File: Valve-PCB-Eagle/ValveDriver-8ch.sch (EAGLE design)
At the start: 16 parts, among them IC1 ULQ2803A, J10 Valve 3, J11 Valve 2, J12 Valve 1, J4 POWER_JACK, J5 Valve 8, J6 Valve 7, J7 Valve 6, J8 Valve 5, J9 Valve 4

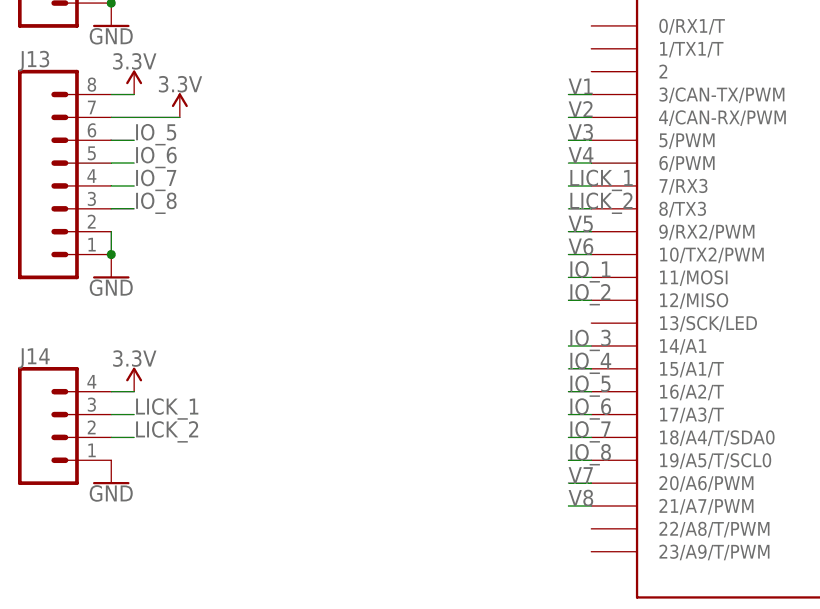
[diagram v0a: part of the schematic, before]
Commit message: [Valve][Teensy] Fix mistaken labeling of Lick1/Lick2 pins
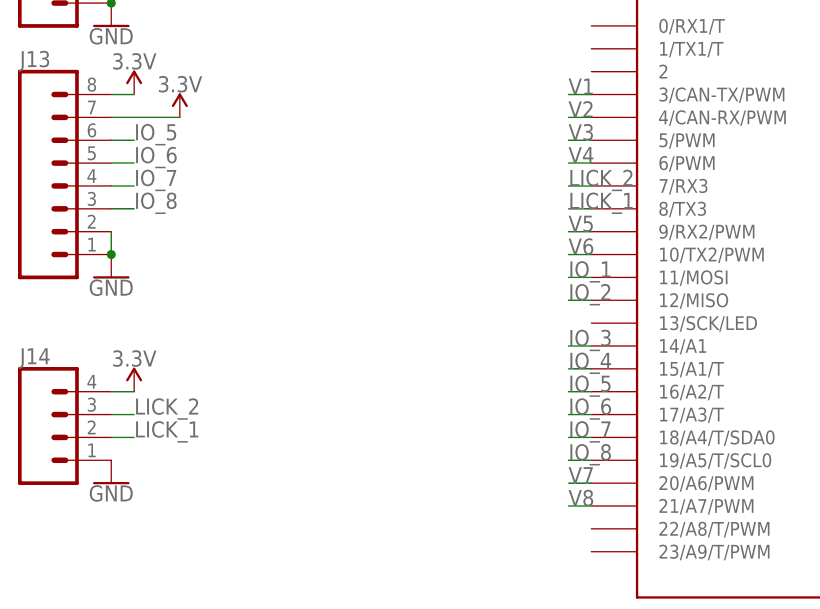
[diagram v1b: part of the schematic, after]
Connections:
- net LICK_1: now also J14.2, U$1.8/TX3; no longer J14.3, U$1.7/RX3
- net LICK_2: now also J14.3, U$1.7/RX3; no longer J14.2, U$1.8/TX3
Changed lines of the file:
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@@
 </segment>
 </net>
-<net name="LICK_1" class="0">
+<net name="LICK_2" class="0">
 <segment>
 <pinref part="U$1" gate="G$1" pin="7/RX3"/>
@@
 </segment>
 </net>
-<net name="LICK_2" class="0">
+<net name="LICK_1" class="0">
 <segment>
 <pinref part="U$1" gate="G$1" pin="8/TX3"/>

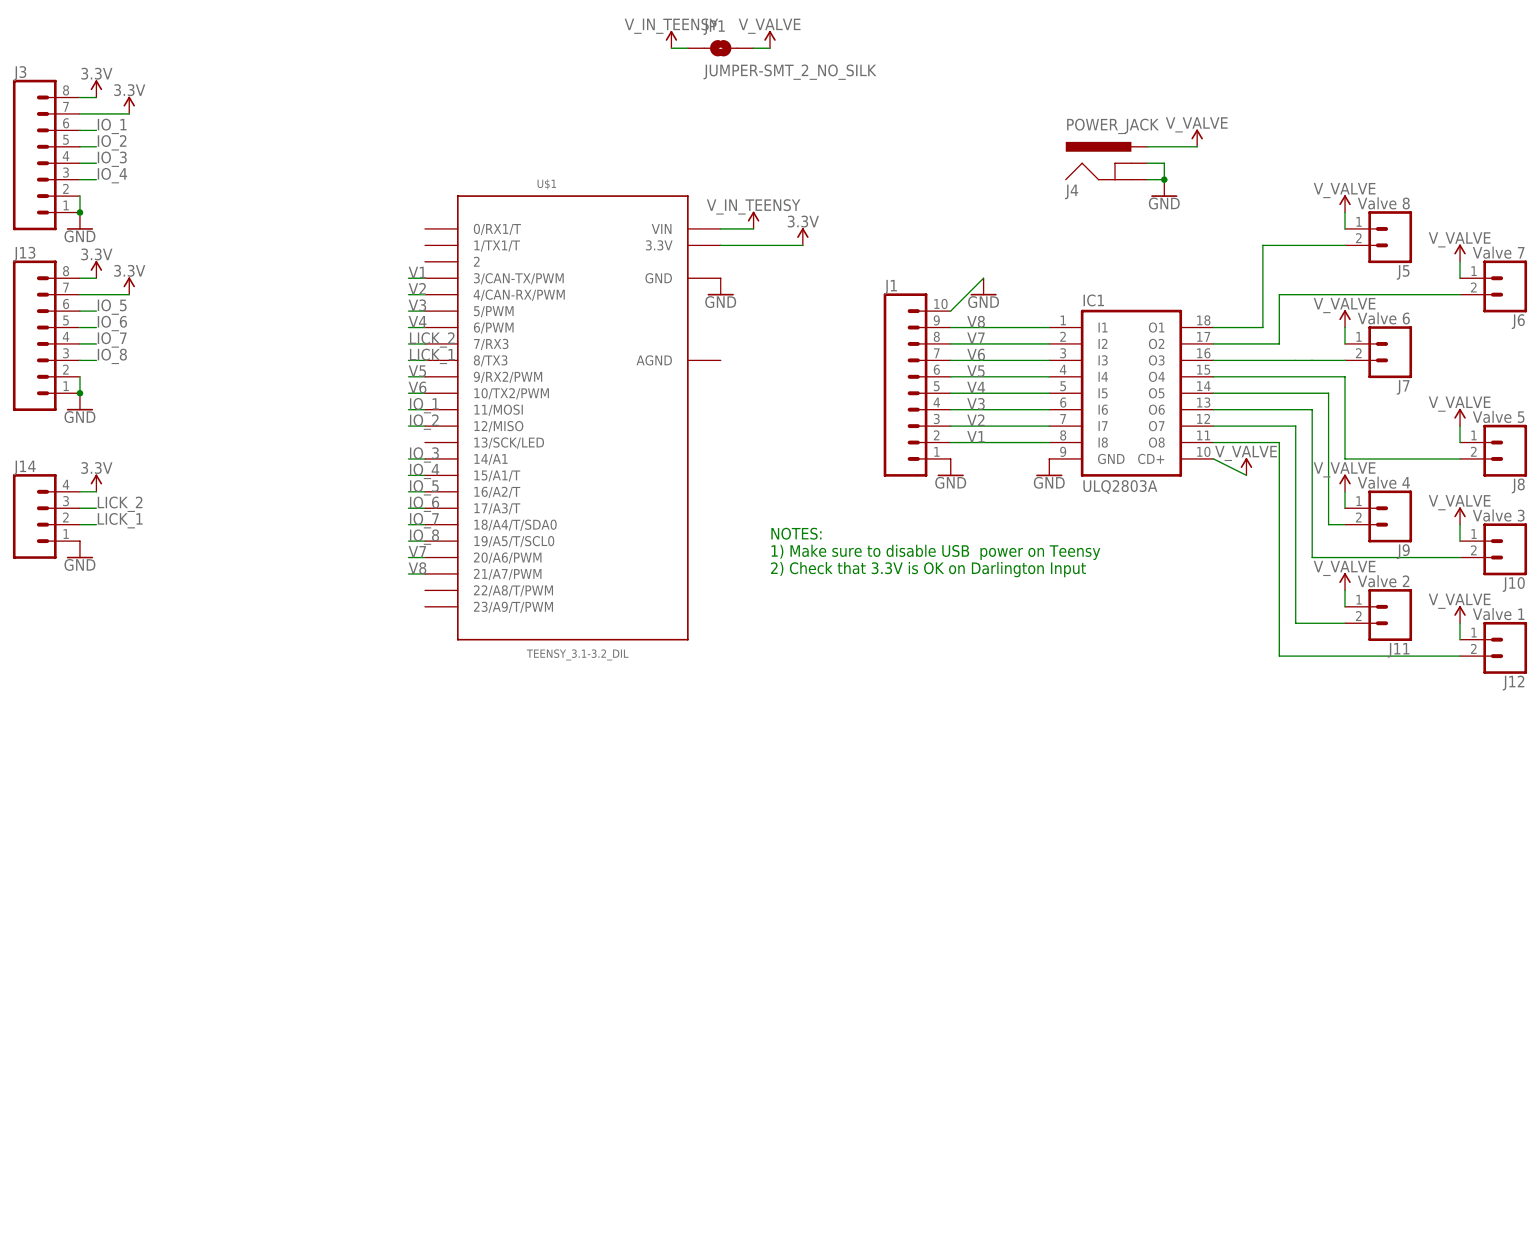
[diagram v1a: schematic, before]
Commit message: [Valve] Add 5V to screw term (fixes #6)
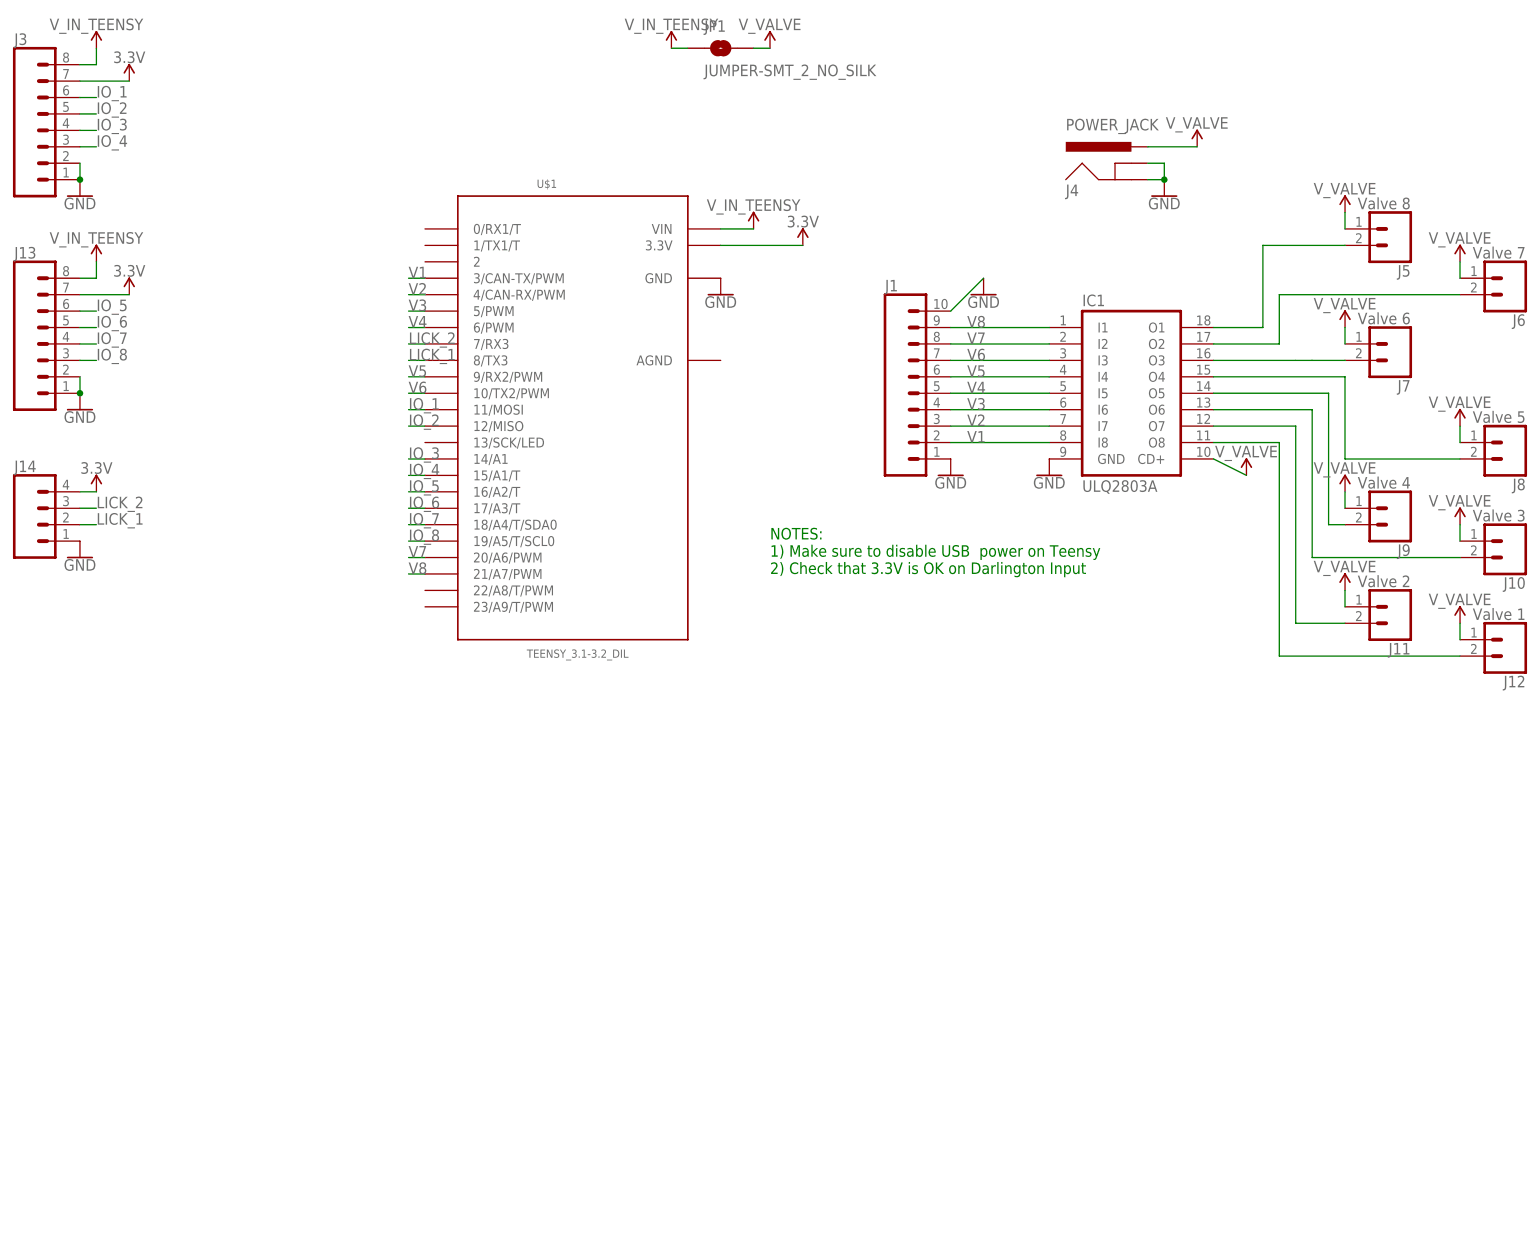
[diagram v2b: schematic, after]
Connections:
- net 3.3V: no longer J13.8, J3.8
- net V_IN_TEENSY: now also J13.8, J3.8
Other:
- moved on the sheet: J3

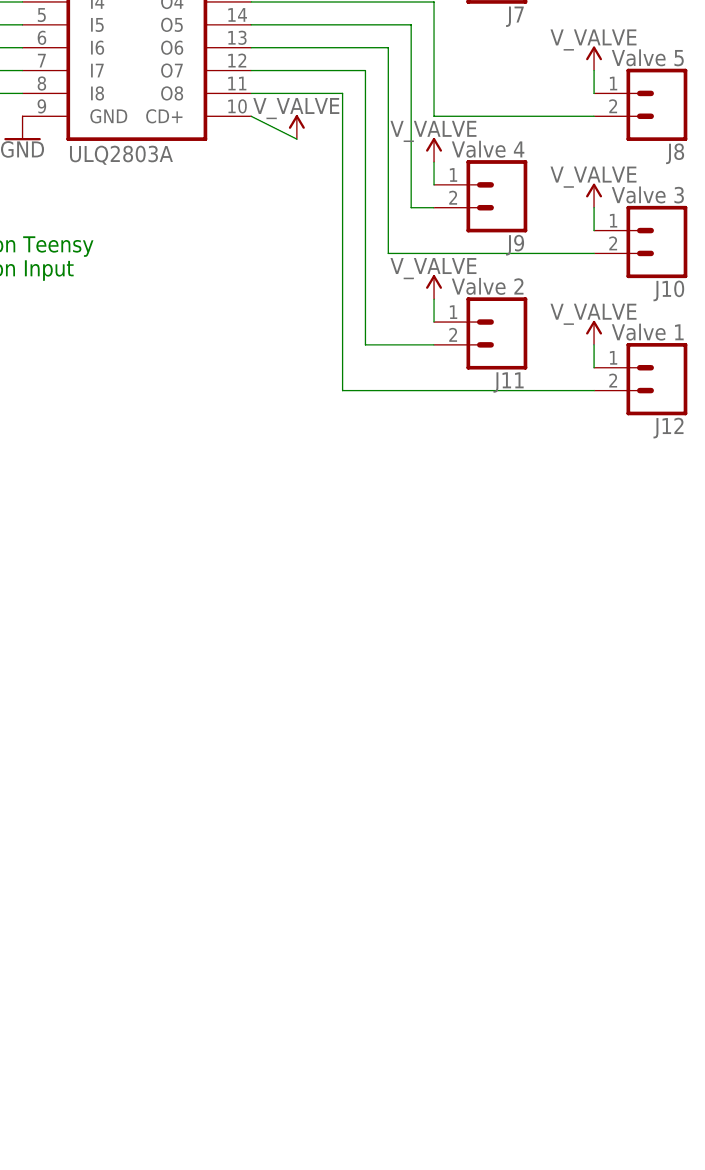
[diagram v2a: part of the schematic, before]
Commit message: [Valve] Add valve manifold connection
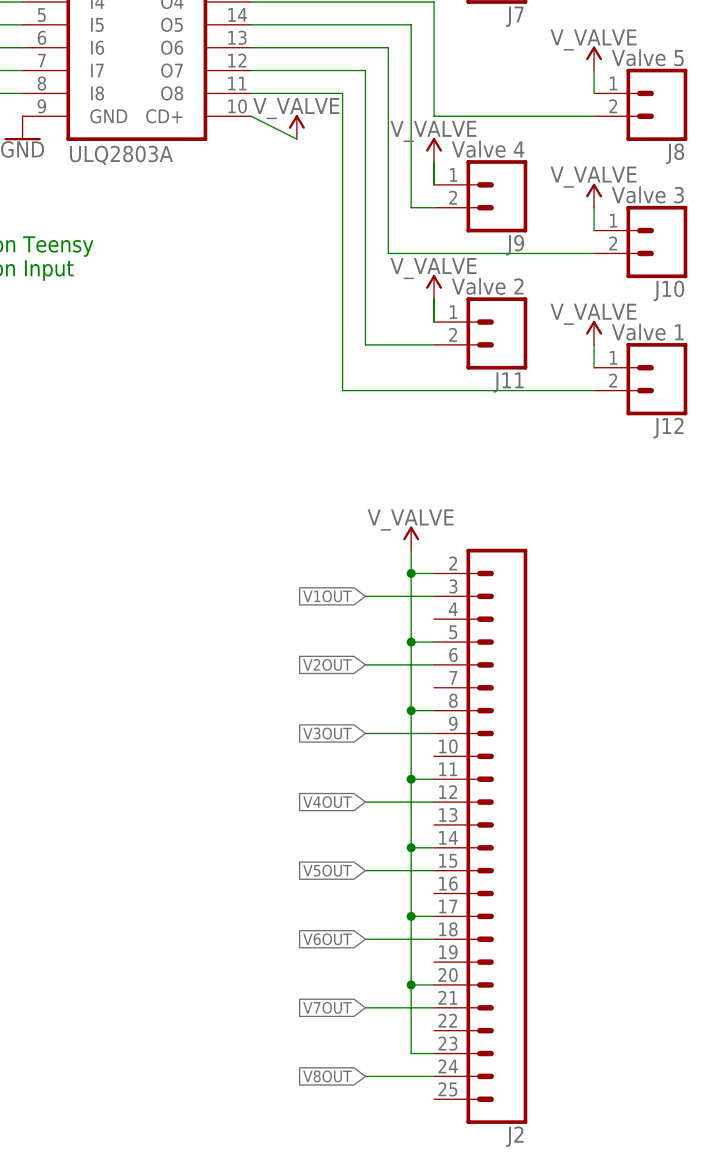
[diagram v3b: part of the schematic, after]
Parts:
- added J2: (no value), SparkFun-Connectors:CONN_24
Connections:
- removed net N$1: IC1.O1, J5.2
- removed net N$2: IC1.O2, J6.2
- removed net N$3: IC1.O3, J7.2
- removed net N$4: IC1.O4, J8.2
- removed net N$5: IC1.O5, J9.2
- removed net N$6: IC1.O6, J10.2
- removed net N$7: IC1.O7, J11.2
- removed net N$8: IC1.O8, J12.2
- new net V1OUT: IC1.O8, J12.2, J2.3
- new net V2OUT: IC1.O7, J11.2, J2.6
- new net V3OUT: IC1.O6, J10.2, J2.9
- new net V4OUT: IC1.O5, J2.12, J9.2
- new net V5OUT: IC1.O4, J2.15, J8.2
- new net V6OUT: IC1.O3, J2.18, J7.2
- new net V7OUT: IC1.O2, J2.21, J6.2
- new net V8OUT: IC1.O1, J2.24, J5.2
- net V_VALVE: now also J2.11, J2.14, J2.17, J2.2, J2.20, J2.23, J2.5, J2.8
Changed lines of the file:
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@@
 <?xml version="1.0" encoding="utf-8"?>
 <!DOCTYPE eagle SYSTEM "eagle.dtd">
-<eagle version="9.2.2">
+<eagle version="9.3.0">
 <drawing>
 <settings>
@@
 <part name="SUPPLY2" library="SparkFun-PowerSymbols" library_urn="urn:adsk.eagle:library:530" deviceset="V_USB" device="" value="V_IN_TEENSY"/>
 <part name="V_IN_TEENSY" library="SparkFun-PowerSymbols" library_urn="urn:adsk.eagle:library:530" deviceset="V_USB" device="" value="V_IN_TEENSY"/>
+<part name="J2" library="SparkFun-Connectors" library_urn="urn:adsk.eagle:library:513" deviceset="CONN_24" device="" package3d_urn="urn:adsk.eagle:package:38202/1"/>
+<part name="SUPPLY13" library="SparkFun-PowerSymbols" library_urn="urn:adsk.eagle:library:530" deviceset="VCC_1" device="" value="V_VALVE"/>
 </parts>
 <sheets>
@@
 <attribute name="VALUE" x="-114.3" y="86.614" size="1.778" layer="96" align="bottom-center"/>
 </instance>
+<instance part="J2" gate="G$1" x="86.36" y="-25.4" smashed="yes" rot="R180">
+<attribute name="VALUE" x="88.9" y="7.366" size="1.778" layer="96" font="vector" rot="R180"/>
+<attribute name="NAME" x="88.9" y="-58.928" size="1.778" layer="95" font="vector" rot="R180"/>
+</instance>
+<instance part="SUPPLY13" gate="G$2" x="76.2" y="5.08" smashed="yes">
+<attribute name="VALUE" x="76.2" y="7.874" size="1.778" layer="96" align="bottom-center"/>
+</instance>
 </instances>
 <busses>
@@
 <pinref part="SUPPLY8" gate="G$2" pin="VCC_1"/>
 <wire x1="78.74" y1="45.72" x2="78.74" y2="48.26" width="0.1524" layer="91"/>
+<wire x1="78.74" y1="45.72" x2="78.74" y2="48.26" width="0.1524" layer="91"/>
 </segment>
 <segment>
@@
 <pinref part="SUPPLY9" gate="G$2" pin="VCC_1"/>
 <wire x1="78.74" y1="30.48" x2="78.74" y2="33.02" width="0.1524" layer="91"/>
+<wire x1="78.74" y1="30.48" x2="78.74" y2="33.02" width="0.1524" layer="91"/>
 </segment>
 <segment>
@@
 <wire x1="-10.16" y1="116.84" x2="-12.7" y2="116.84" width="0.1524" layer="91"/>
 </segment>
-</net>
-<net name="N$1" class="1">
+<segment>
+<pinref part="SUPPLY13" gate="G$2" pin="VCC_1"/>
+<wire x1="76.2" y1="5.08" x2="76.2" y2="2.54" width="0.1524" layer="91"/>
+<pinref part="J2" gate="G$1" pin="2"/>
+<wire x1="76.2" y1="2.54" x2="78.74" y2="2.54" width="0.1524" layer="91"/>
+<pinref part="J2" gate="G$1" pin="5"/>
+<wire x1="76.2" y1="2.54" x2="76.2" y2="-5.08" width="0.1524" layer="91"/>
+<wire x1="76.2" y1="-5.08" x2="78.74" y2="-5.08" width="0.1524" layer="91"/>
+<junction x="76.2" y="2.54"/>
+<pinref part="J2" gate="G$1" pin="8"/>
+<wire x1="76.2" y1="-5.08" x2="76.2" y2="-12.7" width="0.1524" layer="91"/>
+<wire x1="76.2" y1="-12.7" x2="78.74" y2="-12.7" width="0.1524" layer="91"/>
+<junction x="76.2" y="-5.08"/>
+<pinref part="J2" gate="G$1" pin="11"/>
+<wire x1="76.2" y1="-12.7" x2="76.2" y2="-20.32" width="0.1524" layer="91"/>
+<wire x1="76.2" y1="-20.32" x2="78.74" y2="-20.32" width="0.1524" layer="91"/>
+<junction x="76.2" y="-12.7"/>
+<pinref part="J2" gate="G$1" pin="14"/>
+<wire x1="76.2" y1="-20.32" x2="76.2" y2="-27.94" width="0.1524" layer="91"/>
+<wire x1="76.2" y1="-27.94" x2="78.74" y2="-27.94" width="0.1524" layer="91"/>
+<junction x="76.2" y="-20.32"/>
+<pinref part="J2" gate="G$1" pin="17"/>
+<wire x1="76.2" y1="-27.94" x2="76.2" y2="-35.56" width="0.1524" layer="91"/>
+<wire x1="76.2" y1="-35.56" x2="78.74" y2="-35.56" width="0.1524" layer="91"/>
+<junction x="76.2" y="-27.94"/>
+<pinref part="J2" gate="G$1" pin="20"/>
+<wire x1="76.2" y1="-35.56" x2="76.2" y2="-43.18" width="0.1524" layer="91"/>
+<wire x1="76.2" y1="-43.18" x2="78.74" y2="-43.18" width="0.1524" layer="91"/>
+<junction x="76.2" y="-35.56"/>
+<pinref part="J2" gate="G$1" pin="23"/>
+<wire x1="76.2" y1="-43.18" x2="76.2" y2="-50.8" width="0.1524" layer="91"/>
+<wire x1="76.2" y1="-50.8" x2="78.74" y2="-50.8" width="0.1524" layer="91"/>
+<junction x="76.2" y="-43.18"/>
+</segment>
+</net>
+<net name="V8OUT" class="1">
 <segment>
 <pinref part="IC1" gate="G$1" pin="O1"/>
@@
 <wire x1="66.04" y1="86.36" x2="78.74" y2="86.36" width="0.1524" layer="91"/>
 </segment>
-</net>
-<net name="N$2" class="1">
+<segment>
+<pinref part="J2" gate="G$1" pin="24"/>
+<wire x1="78.74" y1="-53.34" x2="71.12" y2="-53.34" width="0.1524" layer="91"/>
+<label x="71.12" y="-53.34" size="1.27" layer="95" rot="R180" xref="yes"/>
+</segment>
+</net>
+<net name="V7OUT" class="1">
 <segment>
 <pinref part="IC1" gate="G$1" pin="O2"/>
@@
 <wire x1="68.58" y1="78.74" x2="96.52" y2="78.74" width="0.1524" layer="91"/>
 </segment>
-</net>
-<net name="N$3" class="1">
+<segment>
+<pinref part="J2" gate="G$1" pin="21"/>
+<wire x1="78.74" y1="-45.72" x2="71.12" y2="-45.72" width="0.1524" layer="91"/>
+<label x="71.12" y="-45.72" size="1.27" layer="95" rot="R180" xref="yes"/>
+</segment>
+</net>
+<net name="V6OUT" class="1">
 <segment>
 <pinref part="IC1" gate="G$1" pin="O3"/>
@@
 <wire x1="73.66" y1="68.58" x2="71.12" y2="68.58" width="0.1524" layer="91"/>
 </segment>
-</net>
-<net name="N$4" class="1">
+<segment>
+<pinref part="J2" gate="G$1" pin="18"/>
+<wire x1="78.74" y1="-38.1" x2="71.12" y2="-38.1" width="0.1524" layer="91"/>
+<label x="71.12" y="-38.1" size="1.27" layer="95" rot="R180" xref="yes"/>
+</segment>
+</net>
+<net name="V5OUT" class="1">
 <segment>
 <pinref part="IC1" gate="G$1" pin="O4"/>
@@
 <wire x1="78.74" y1="53.34" x2="96.52" y2="53.34" width="0.1524" layer="91"/>
 </segment>
-</net>
-<net name="N$5" class="1">
+<segment>
+<pinref part="J2" gate="G$1" pin="15"/>
+<wire x1="78.74" y1="-30.48" x2="71.12" y2="-30.48" width="0.1524" layer="91"/>
+<label x="71.12" y="-30.48" size="1.27" layer="95" rot="R180" xref="yes"/>
+</segment>
+</net>
+<net name="V4OUT" class="1">
 <segment>
 <pinref part="IC1" gate="G$1" pin="O5"/>
@@
 <wire x1="76.2" y1="63.5" x2="58.42" y2="63.5" width="0.1524" layer="91"/>
 </segment>
-</net>
-<net name="N$6" class="1">
+<segment>
+<pinref part="J2" gate="G$1" pin="12"/>
+<wire x1="78.74" y1="-22.86" x2="71.12" y2="-22.86" width="0.1524" layer="91"/>
+<label x="71.12" y="-22.86" size="1.27" layer="95" rot="R180" xref="yes"/>
+</segment>
+</net>
+<net name="V3OUT" class="1">
 <segment>
 <pinref part="IC1" gate="G$1" pin="O6"/>
@@
 <wire x1="73.66" y1="38.1" x2="96.52" y2="38.1" width="0.1524" layer="91"/>
 </segment>
-</net>
-<net name="N$7" class="1">
+<segment>
+<pinref part="J2" gate="G$1" pin="9"/>
+<wire x1="78.74" y1="-15.24" x2="71.12" y2="-15.24" width="0.1524" layer="91"/>
+<label x="71.12" y="-15.24" size="1.27" layer="95" rot="R180" xref="yes"/>
+</segment>
+</net>
+<net name="V2OUT" class="1">
 <segment>
 <pinref part="IC1" gate="G$1" pin="O7"/>
@@
 <wire x1="71.12" y1="27.94" x2="71.12" y2="58.42" width="0.1524" layer="91"/>
 </segment>
-</net>
-<net name="N$8" class="1">
+<segment>
+<pinref part="J2" gate="G$1" pin="6"/>
+<wire x1="78.74" y1="-7.62" x2="71.12" y2="-7.62" width="0.1524" layer="91"/>
+<label x="71.12" y="-7.62" size="1.27" layer="95" rot="R180" xref="yes"/>
+</segment>
+</net>
+<net name="V1OUT" class="1">
 <segment>
 <pinref part="IC1" gate="G$1" pin="O8"/>
@@
 <wire x1="68.58" y1="22.86" x2="96.52" y2="22.86" width="0.1524" layer="91"/>
 </segment>
-</net>
+<segment>
+<pinref part="J2" gate="G$1" pin="3"/>
+<wire x1="78.74" y1="0" x2="71.12" y2="0" width="0.1524" layer="91"/>
+<label x="71.12" y="0" size="1.27" layer="95" rot="R180" xref="yes"/>
+</segment>
+</net>
